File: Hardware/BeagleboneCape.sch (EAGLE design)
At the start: 3 parts

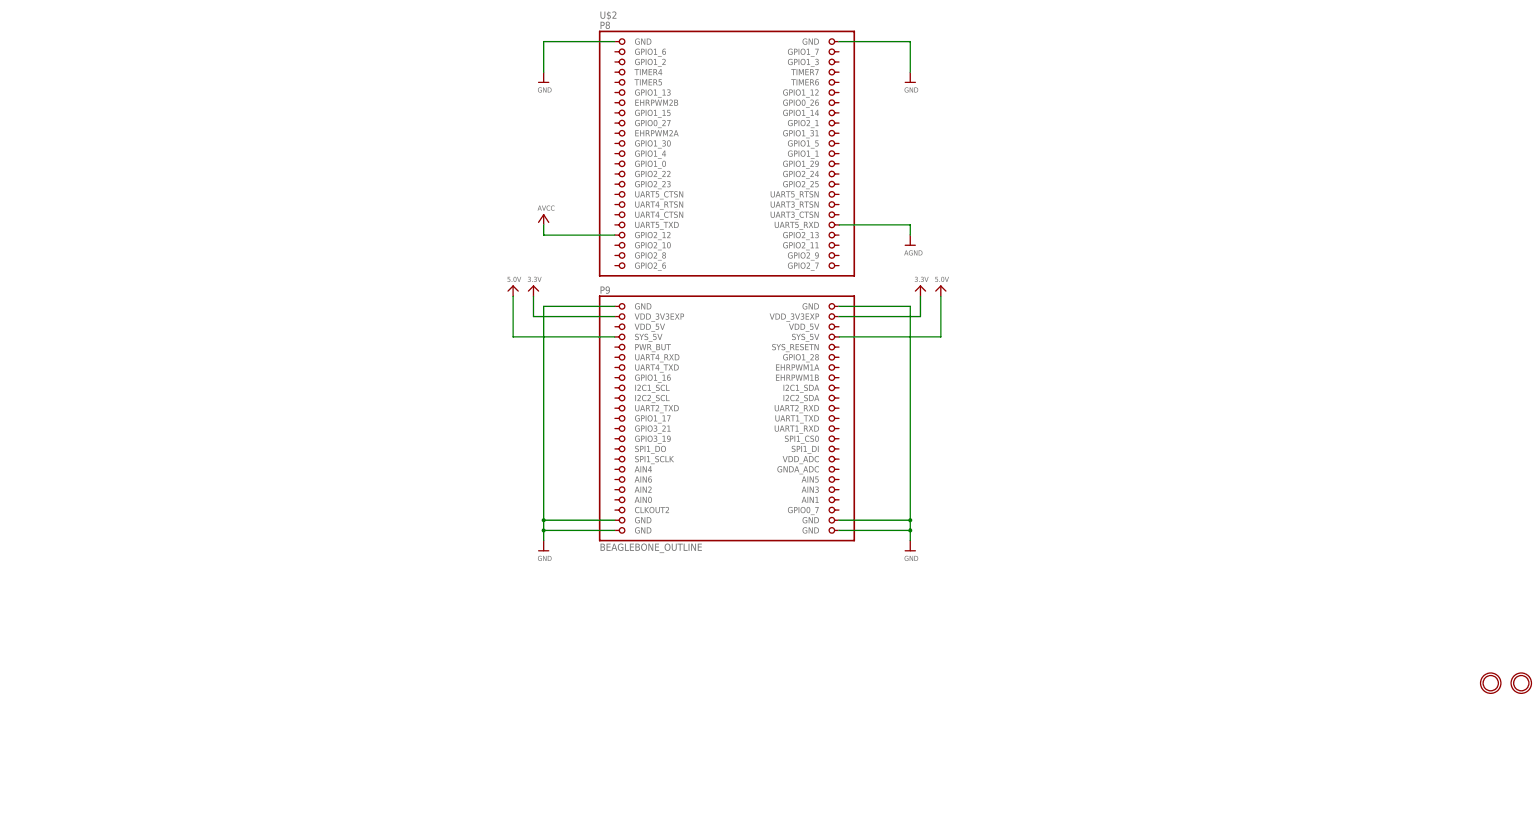
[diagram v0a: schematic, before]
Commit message: Removed Adafruit Beaglebone Sample ( was used for reference only). Finished beaglebone board Connecting NRF24L01 through SPI1 and Xbee to UART1 Generated PCB Pdf Files.
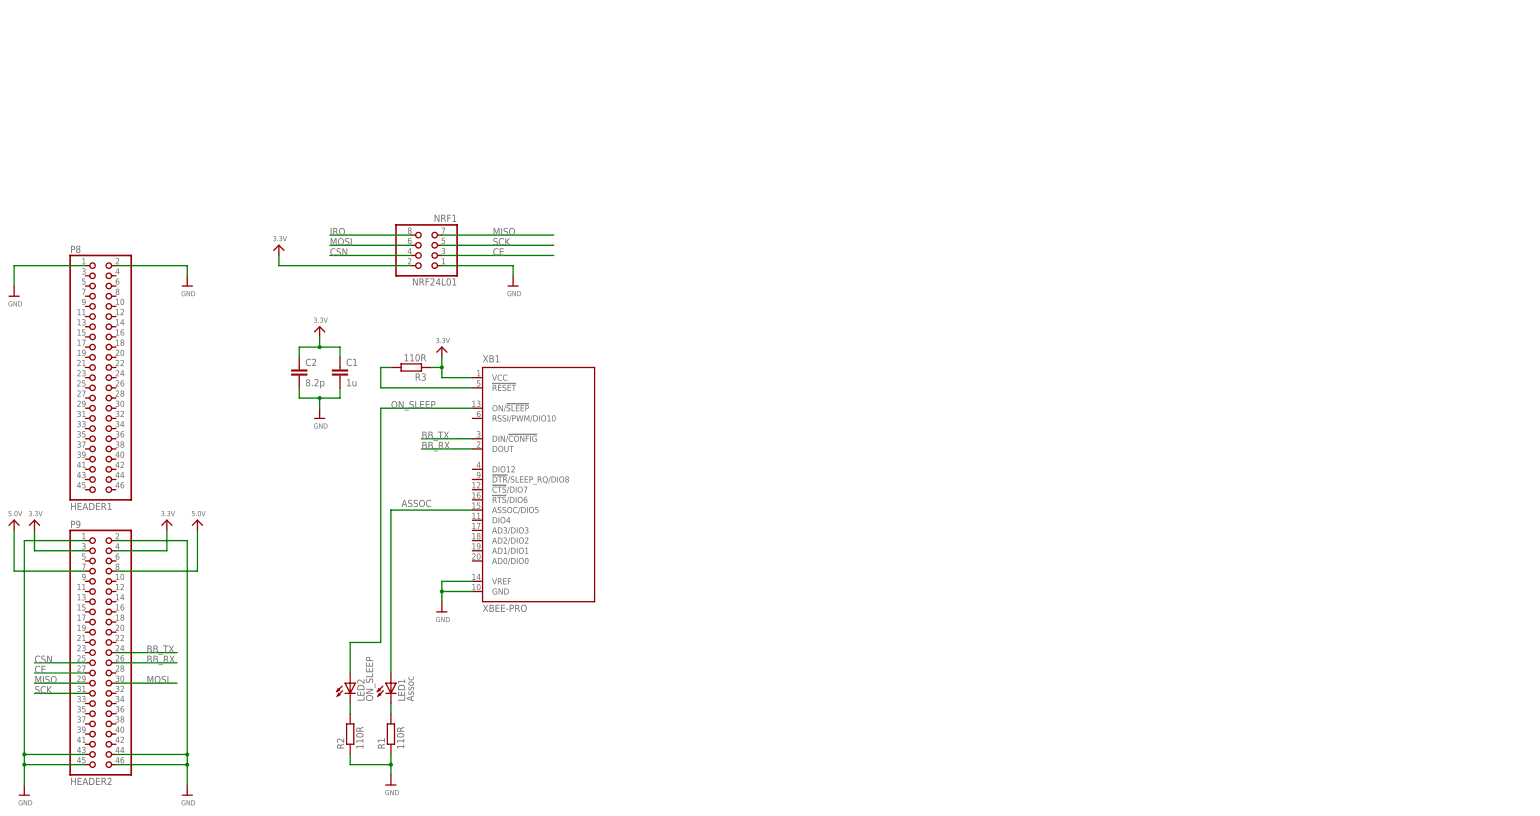
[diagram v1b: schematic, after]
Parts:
- removed U$2: BEAGLEBONE_OUTLINE, microbuilder:BEAGLEBONE_OUTLINE
- removed U$22, U$23: MOUNTINGHOLE3.0THIN, microbuilder:MOUNTINGHOLE3.0THIN
- added C1: 1u, rcl:C-EU025-025X050
- added C2: 8.2p, rcl:C-EU025-025X050
- added LED1: Assoc, led:LED5MM
- added LED2: ON_SLEEP, led:LED5MM
- added NRF24L01: NRF1, pinhead:PINHD-2X4
- added P8: HEADER1, 2X23Header:PINHD-2X24
- added P9: HEADER2, 2X23Header:PINHD-2X24
- added R1, R2, R3: 110R, rcl:R-EU_0207/7
- added XB1: XBEE-PRO, xbee:XBEE-PRO
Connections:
- removed net AGND: U$2.UART5_RXD
- removed net AVCC: U$2.GPIO2_12
- new net ASSOC: LED1.A, XB1.ASSOC/DIO5
- new net BB_RX: P9.26, XB1.DOUT
- new net BB_TX: P9.24, XB1.DIN/!CONFIG
- new net CE: NRF24L01.3, P9.27
- new net CSN: NRF24L01.4, P9.25
- new net IRQ: NRF24L01.8
- new net MISO: NRF24L01.7, P9.29
- new net MOSI: NRF24L01.6, P9.30
- new net N$1: LED1.C, R1.2
- new net N$2: R3.2, XB1.!RESET
- new net N$3: LED2.C, R2.2
- new net ON_SLEEP: LED2.A, XB1.ON/!SLEEP
- new net SCK: NRF24L01.5, P9.31
- net 3.3V: now also C1.1, C2.1, NRF24L01.2, P9.3, P9.4, R3.1, XB1.VCC; no longer U$2.VDD_3V3EXP@1, U$2.VDD_3V3EXP@2
- net 5.0V: now also P9.7, P9.8; no longer U$2.SYS_5V@1, U$2.SYS_5V@2
- net GND: now also C1.2, C2.2, NRF24L01.1, P8.1, P8.2, P9.1, P9.2, P9.43, P9.44, P9.45, P9.46, R1.1, R2.1, XB1.GND, XB1.VREF; no longer U$2.GND@1, U$2.GND@2, U$2.GND@3, U$2.GND@4, U$2.GND@5, U$2.GND@6, U$2.GND@7, U$2.GND@8
